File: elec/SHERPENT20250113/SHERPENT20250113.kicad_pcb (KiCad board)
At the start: 4 copper layers, 130.2 x 60.2 mm, 95 parts, among them J1 2137160001, J2 Conn_01x02_Socket, J3 Conn_01x03_Socket, J4 Conn_01x03_Socket, Q1 NMOS, Q2 PMOS, SW1 SW_Push, U1 AN034_ANTENNA, U2 MCP73831T-2ACI_OT, U3 TPS61288LRQQR, U4 TPS7A2633DRVR, U5 LM66200DRLR, U6 ESP32-C3, U7 W25Q128JVS, Y1 40MHz

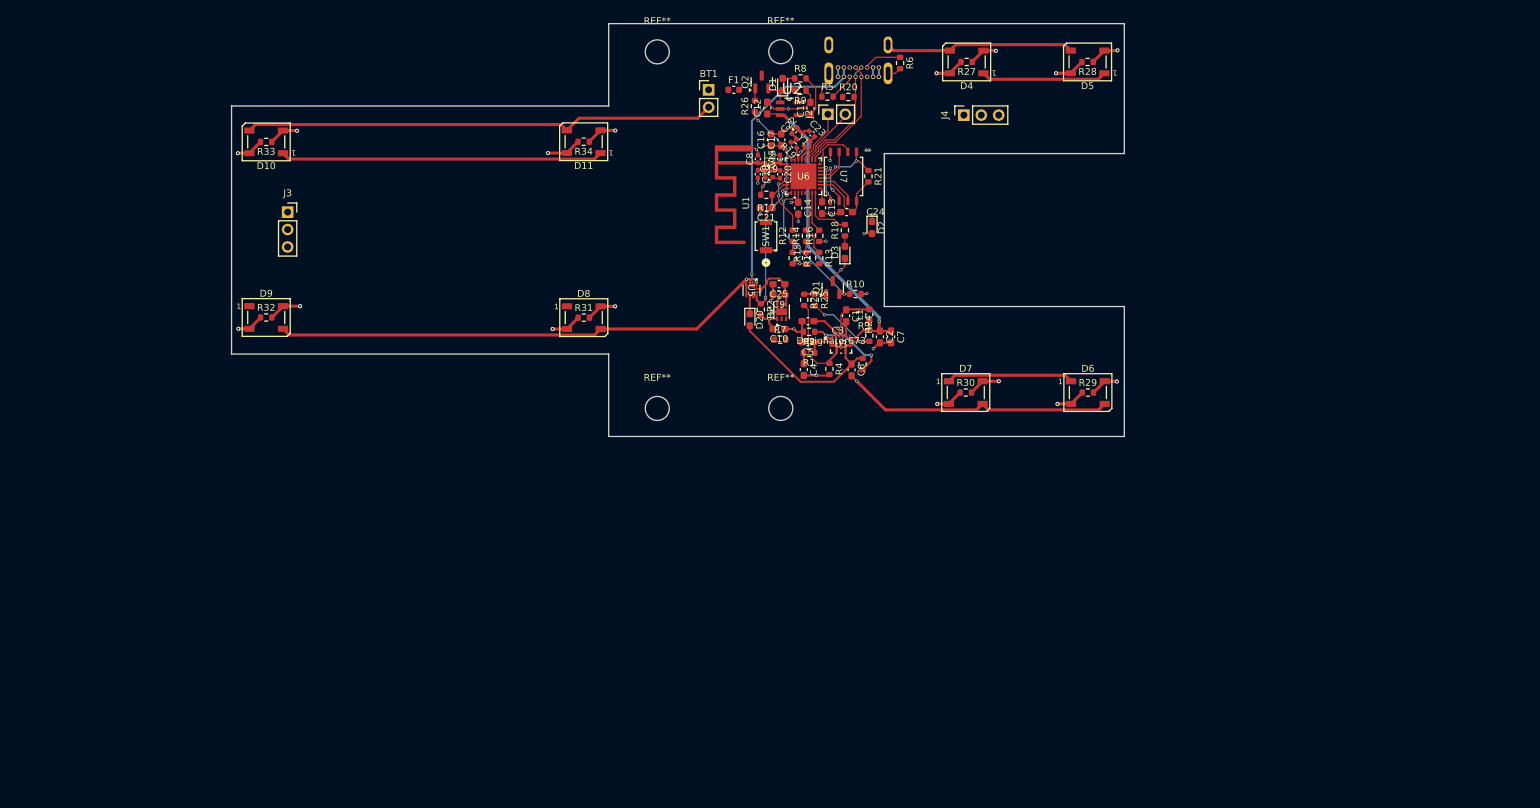
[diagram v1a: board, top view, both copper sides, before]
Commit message: rough rgb placement
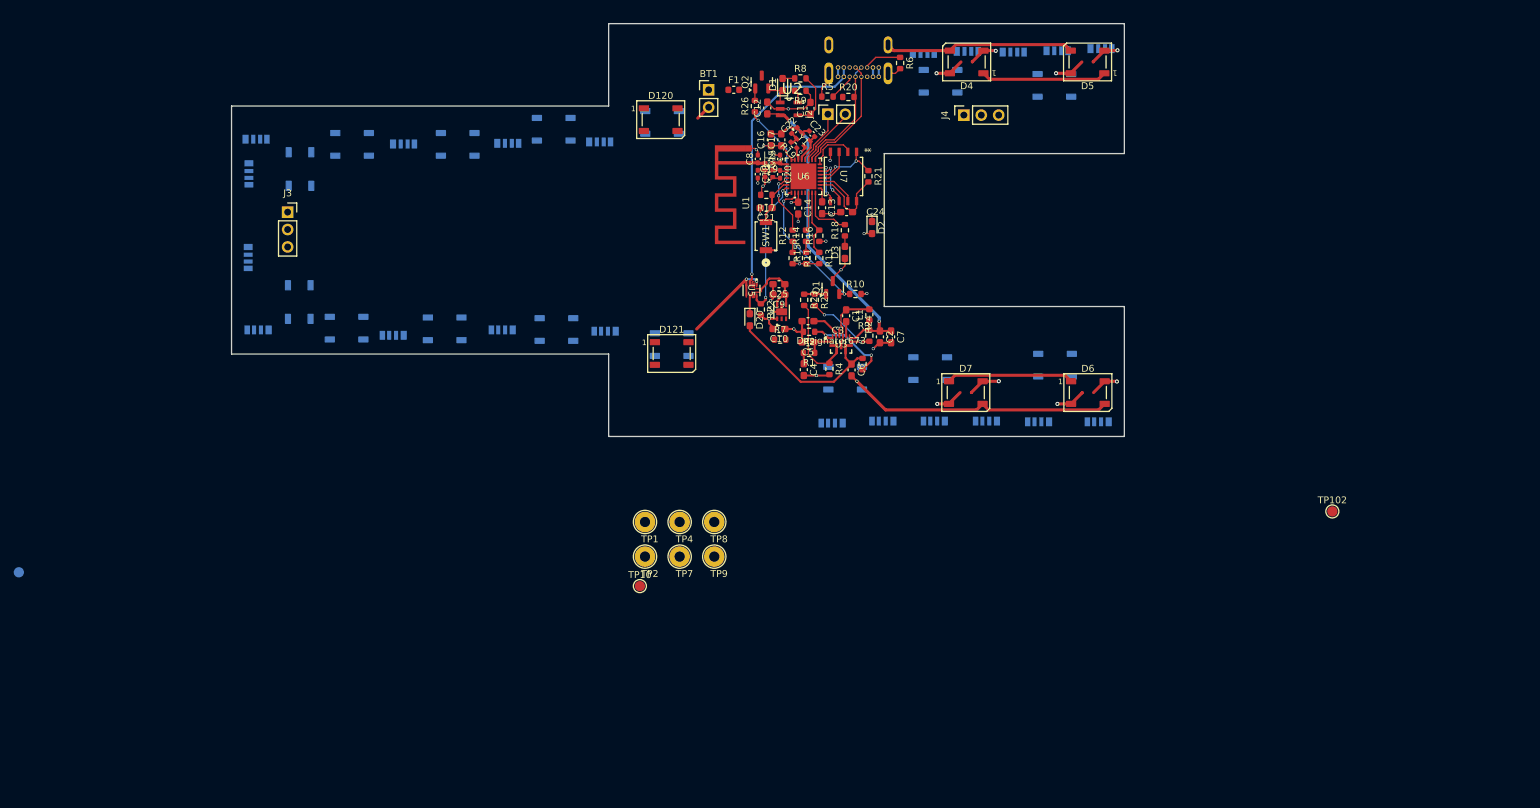
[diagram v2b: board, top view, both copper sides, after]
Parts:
- removed R27, R28, R29, R30, R31, R32, R33, R34: 0, Resistor_SMD:R_0603_1608Metric
- removed REF** (x4): MountingHole_3.5mm, MountingHole:MountingHole_3.5mm
- added D101: WS2812B, LED_SMD:LED_WS2812B_PLCC4_5.0x5.0mm_P3.2mm, B.Cu at (108.0, 117.4)
- added D102: WS2812B, LED_SMD:LED_WS2812B_PLCC4_5.0x5.0mm_P3.2mm, B.Cu at (141.1, 119.7)
- added D103: WS2812B, LED_SMD:LED_WS2812B_PLCC4_5.0x5.0mm_P3.2mm, B.Cu at (139.7, 87.3)
- added D104: WS2812B, LED_SMD:LED_WS2812B_PLCC4_5.0x5.0mm_P3.2mm, B.Cu at (178.8, 123.2)
- added D105: WS2812B, LED_SMD:LED_WS2812B_PLCC4_5.0x5.0mm_P3.2mm, B.Cu at (197.0, 122.7)
- added D106: WS2812B, LED_SMD:LED_WS2812B_PLCC4_5.0x5.0mm_P3.2mm, B.Cu at (93.7, 117.3)
- added D107: WS2812B, LED_SMD:LED_WS2812B_PLCC4_5.0x5.0mm_P3.2mm, B.Cu at (124.3, 117.5)
- added D108: WS2812B, LED_SMD:LED_WS2812B_PLCC4_5.0x5.0mm_P3.2mm, B.Cu at (123.9, 88.3)
- added D109: WS2812B4020, Library:WS2812B4020, B.Cu at (131.4, 118.6)
- added D110: WS2812B4020, Library:WS2812B4020, B.Cu at (171.9, 131.7)
- added D111: WS2812B4020, Library:WS2812B4020, B.Cu at (187.0, 131.7)
- added D112: WS2812B4020, Library:WS2812B4020, B.Cu at (194.6, 131.8)
- added D113: WS2812B4020, Library:WS2812B4020, B.Cu at (203.3, 131.8)
- added D114: WS2812B4020, Library:WS2812B4020, B.Cu at (116.4, 118.4)
- added D115: WS2812B4020, Library:WS2812B4020, B.Cu at (164.5, 132.0)
- added D116: WS2812B4020, Library:WS2812B4020, B.Cu at (179.4, 131.7)
- added D117: WS2812B, LED_SMD:LED_WS2812B_PLCC4_5.0x5.0mm_P3.2mm, B.Cu at (196.9, 81.9)
- added D118: WS2812B, LED_SMD:LED_WS2812B_PLCC4_5.0x5.0mm_P3.2mm, B.Cu at (180.3, 81.3)
- added D119: WS2812B, LED_SMD:LED_WS2812B_PLCC4_5.0x5.0mm_P3.2mm, B.Cu at (166.4, 124.6)
- added D12: WS2812B4020, Library:WS2812B4020, B.Cu at (80.5, 88.9)
- added D120: WS2812B, LED_SMD:LED_WS2812B_PLCC4_5.0x5.0mm_P3.2mm, F.Cu at (139.5, 86.9)
- added D121: WS2812B, LED_SMD:LED_WS2812B_PLCC4_5.0x5.0mm_P3.2mm, F.Cu at (141.1, 121.0)
- added D125: WS2812B4020, Library:WS2812B4020, B.Cu at (203.7, 75.7)
- added D126: WS2812B4020, Library:WS2812B4020, B.Cu at (197.3, 76.0)
- added D127: WS2812B4020, Library:WS2812B4020, B.Cu at (190.9, 76.2)
- added D128: WS2812B4020, Library:WS2812B4020, B.Cu at (184.2, 76.1)
- added D129: WS2812B4020, Library:WS2812B4020, B.Cu at (177.8, 76.4)
- added D13: WS2812B4020, Library:WS2812B4020, B.Cu at (80.3, 94.8)
- added D14: WS2812B4020, Library:WS2812B4020, B.Cu at (80.2, 107.0)
- added D15: WS2812B4020, Library:WS2812B4020, B.Cu at (80.8, 118.4)
- added D16: WS2812B4020, Library:WS2812B4020, B.Cu at (100.5, 119.2)
- added D17: WS2812B4020, Library:WS2812B4020, B.Cu at (102.0, 89.6)
- added D18: WS2812B4020, Library:WS2812B4020, B.Cu at (117.2, 89.5)
- added D19: WS2812B4020, Library:WS2812B4020, B.Cu at (130.6, 89.3)
- added TP1: TestPoint, TestPoint:TestPoint_Loop_D2.54mm_Drill1.5mm_Beaded, F.Cu at (137.2, 145.6)
- added TP10: TestPoint, TestPoint:TestPoint_Pad_D1.5mm, F.Cu at (136.5, 154.9)
- added TP101: TestPoint, TestPoint:TestPoint_Pad_D1.5mm, B.Cu at (45.9, 152.9)
- added TP102: TestPoint, TestPoint:TestPoint_Pad_D1.5mm, F.Cu at (237.4, 144.0)
- added TP2: TestPoint, TestPoint:TestPoint_Loop_D2.54mm_Drill1.5mm_Beaded, F.Cu at (137.2, 150.6)
- added TP4: TestPoint, TestPoint:TestPoint_Loop_D2.54mm_Drill1.5mm_Beaded, F.Cu at (142.3, 145.6)
- added TP7: TestPoint, TestPoint:TestPoint_Loop_D2.54mm_Drill1.5mm_Beaded, F.Cu at (142.3, 150.6)
- added TP8: TestPoint, TestPoint:TestPoint_Loop_D2.54mm_Drill1.5mm_Beaded, F.Cu at (147.3, 145.6)
- added TP9: TestPoint, TestPoint:TestPoint_Loop_D2.54mm_Drill1.5mm_Beaded, F.Cu at (147.3, 150.6)
- D10, D11, D8, D9: moved to B.Cu
- moved D11 41.6 mm to (86.9, 94.1), turned to -90 degrees
- moved D8 41.5 mm to (86.8, 113.5), turned to 90 degrees
- moved D9 37.6 mm to (109.9, 90.5), turned to 180 degrees
- moved D10 12.5 mm to (94.5, 90.5), turned to 0 degrees
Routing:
- net GND: track 284.2 -> 156.3 mm
- net Net-(D8-DOUT): track 47.4 -> 0.00 mm, vias 2 -> 0
- net Net-(D10-DOUT): track 47.4 -> 0.00 mm, vias 2 -> 0
- net +5V: track 83.9 -> 36.9 mm
- net Net-(D10-DIN): track 33.6 -> 0.00 mm, vias 2 -> 0
- net Net-(D7-DOUT): track 61.4 -> 36.9 mm, vias 2 -> 1
- net Net-(D11-DOUT): track 4.50 -> 0.00 mm, vias 1 -> 0

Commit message: Quicksave. J'ai mis le connecteur du bon bord. Va falloir flipper le trou de place pis recheck le routing. Stayon circuit en cours
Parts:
- J1: moved to F.Cu
- moved R5 7.40 mm to (171.2, 84.1), turned to 180 degrees
- moved F1 0.85 mm to (150.2, 83.4), turned to -90 degrees
- turned J1 to 180 degrees
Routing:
- net GND: track 156.3 -> 136.3 mm
- net VBATT: track 47.7 -> 57.5 mm
- net Net-(BT1-+): track 0.00 -> 3.68 mm
- net /USB_ESP32P: track 17.2 -> 19.7 mm

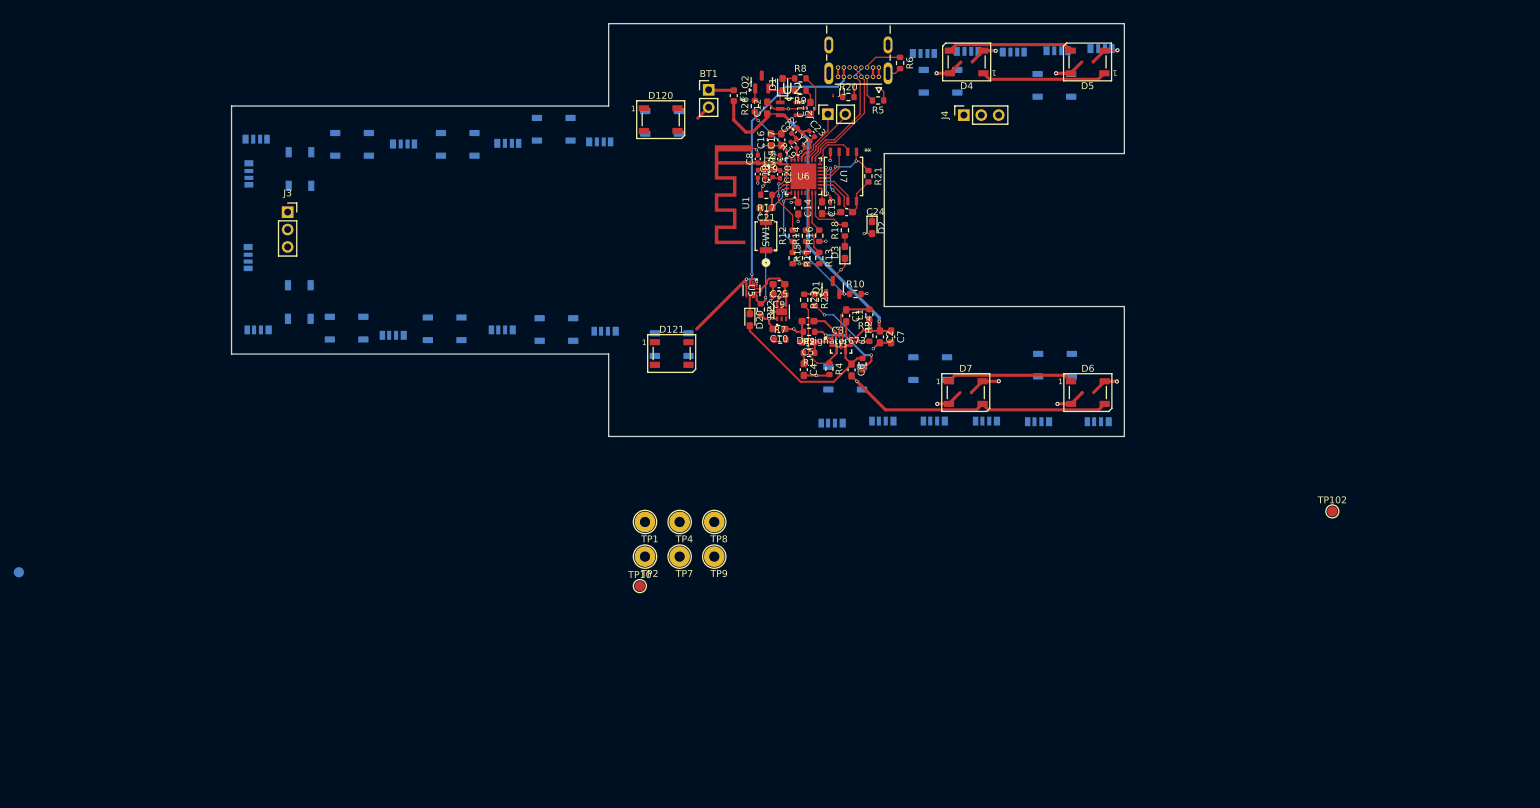
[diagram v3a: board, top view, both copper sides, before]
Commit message: Amélioration du shema. Layout et routing de tout ce qui manquait sauf leds et bouton. Bonne nuit!
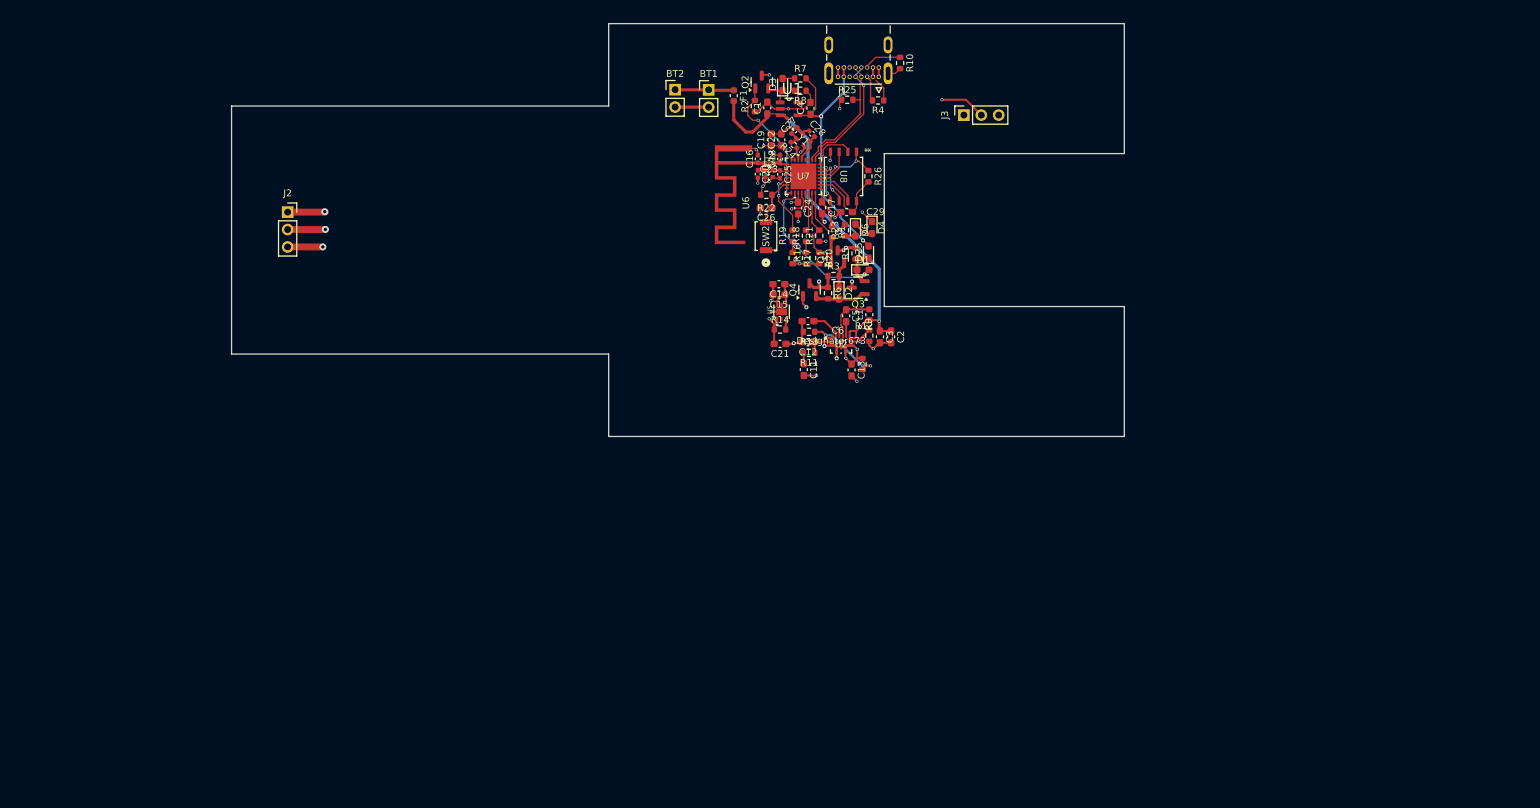
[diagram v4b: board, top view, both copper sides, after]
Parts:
- removed D10, D101, D102, D103, D104, D105, D106, D107, D108, D11, D117, D118, D119, D120, D121, D5, D7, D8, D9: WS2812B, LED_SMD:LED_WS2812B_PLCC4_5.0x5.0mm_P3.2mm
- removed D109, D110, D111, D112, D113, D114, D115, D116, D12, D125, D126, D127, D128, D129, D13, D14, D15, D16, D17, D18, D19: WS2812B4020, Library:WS2812B4020
- removed D20: D, Diode_SMD:D_0603_1608Metric_Pad1.05x0.95mm_HandSolder
- removed the D4 at (184.1, 78.5)
- removed the D6 at (201.8, 126.7)
- removed the J2 at (163.9, 86.1)
- removed the R10 at (167.9, 112.3)
- removed the R22 at (154.1, 114.6)
- removed the R23 at (160.4, 113.2)
- removed the R25 at (162.0, 113.2)
- removed the R4 at (164.1, 123.2)
- removed TP1, TP2, TP4, TP7, TP8, TP9: TestPoint, TestPoint:TestPoint_Loop_D2.54mm_Drill1.5mm_Beaded
- removed TP10, TP101, TP102: TestPoint, TestPoint:TestPoint_Pad_D1.5mm
- removed the U5 at (152.7, 111.8)
- added BT2: Battery_Cell, Connector_PinHeader_2.54mm:PinHeader_1x02_P2.54mm_Vertical, F.Cu at (141.6, 82.5)
- added D1: D_Schottky, LED_SMD:LED_0603_1608Metric_Pad1.05x0.95mm_HandSolder, F.Cu at (169.0, 108.8)
- added D2: D_Schottky, LED_SMD:LED_0603_1608Metric_Pad1.05x0.95mm_HandSolder, F.Cu at (165.5, 112.2)
- added D25: D_Schottky, LED_SMD:LED_0603_1608Metric_Pad1.05x0.95mm_HandSolder, F.Cu at (169.8, 106.2)
- added Q1: NMOS, Package_TO_SOT_SMD:SOT-23, F.Cu at (165.3, 106.9)
- added Q4: PMOS, Package_TO_SOT_SMD:SOT-23, F.Cu at (161.2, 111.7)
- added R1: 10k, Resistor_SMD:R_0603_1608Metric, F.Cu at (164.5, 103.3)
- added R3: 10k, Resistor_SMD:R_0603_1608Metric, F.Cu at (164.7, 109.7)
- added R5: 10k, Resistor_SMD:R_0603_1608Metric, F.Cu at (167.9, 106.4)
- added R6: 10k, Resistor_SMD:R_0603_1608Metric, F.Cu at (163.9, 112.2)
- moved Q3 3.71 mm to (168.3, 111.4), turned to 180 degrees
- moved D6 3.60 mm to (167.9, 103.0), turned to -90 degrees
- moved C21 2.18 mm to (156.9, 119.6)
- moved R14 1.47 mm to (156.9, 117.5)
- moved R25 0.44 mm to (166.7, 84.0)
- renumbered C12 to C1, C4 to C11, C5 to C12, C6 to C13, C25 to C14, C9 to C15, C8 to C16, C13 to C17, C15 to C18, C16 to C19, C7 to C2, C18 to C20, C10 to C21, C17 to C22, C19 to C23, C14 to C24, C20 to C25, C21 to C26, C22 to C27, C23 to C28, C24 to C29, C2 to C3, C11 to C4, C1 to C5, C3 to C6, D1 to D3, D2 to D4, D3 to D6, J3 to J2, J4 to J3, Q1 to Q3, R6 to R10, R1 to R11, R3 to R12, R2 to R13, R7 to R14, R15 to R16, R11 to R17, R14 to R18, R12 to R19, R26 to R2, R13 to R20, R16 to R21, R17 to R22, R18 to R23, R19 to R24, R20 to R25, R21 to R26, R5 to R4, R8 to R7, R9 to R8, R24 to R9, SW1 to SW2, U2 to U1, U3 to U2, U4 to U5, U1 to U6, U6 to U7, U7 to U8
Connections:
- Q2 pad 1: Net-(Q2-D) -> /CHARGE
- Q3 pad 2: /StayOn -> Net-(D1-K)
- R2 pad 1: /CHARGE -> GND
- R2 pad 2: Net-(Q2-D) -> /CHARGE
- R9 pad 1: VBATT -> Net-(Q4-D)
- R9 pad 2: Net-(U3-EN) -> GND
- U2 pad 3: Net-(U3-PGND) -> GND
- U2 pad 6: Net-(U3-EN) -> Net-(Q4-D)
- U7 pad 28: /I2C_DI -> /NEOPX
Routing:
- net +9V: track 24.2 -> 149.7 mm, vias 0 -> 3
- net Net-(D5-DOUT): track 111.5 -> 0.00 mm, vias 2 -> 0
- net /Moteur1_PWM: track 0.00 -> 82.9 mm, vias 0 -> 2
- net /Moteur2_PWM: track 0.00 -> 38.7 mm, vias 0 -> 2
- net GND: track 136.3 -> 174.4 mm, vias 26 -> 28
- net +5V: track 36.9 -> 0.00 mm
- net Net-(D7-DOUT): track 36.9 -> 0.00 mm, vias 1 -> 0
- net /I2C_DO: track 28.9 -> 0.00 mm, vias 1 -> 0
- net +3.3V: track 35.6 -> 57.5 mm, vias 6 -> 9
- net /DIODE_STATE: track 20.1 -> 0.23 mm, vias 2 -> 0
- net Net-(D6-DOUT): track 18.9 -> 0.00 mm, vias 2 -> 0
- net Net-(D4-DOUT): track 18.7 -> 0.00 mm, vias 2 -> 0
- net VBATT: track 57.5 -> 73.3 mm, vias 2 -> 4
- net Net-(Q4-D): track 0.00 -> 15.5 mm, vias 0 -> 2
- net Net-(U3-PGND): track 13.5 -> 0.00 mm
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- removed copper zone on F.Cu, net /VDIODE
